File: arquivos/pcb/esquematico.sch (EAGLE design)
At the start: 14 parts, among them IC1 LM35CZ, IC2 LM35CZ, J1 694108210102, Q1 TIP31, Q2 TIP31

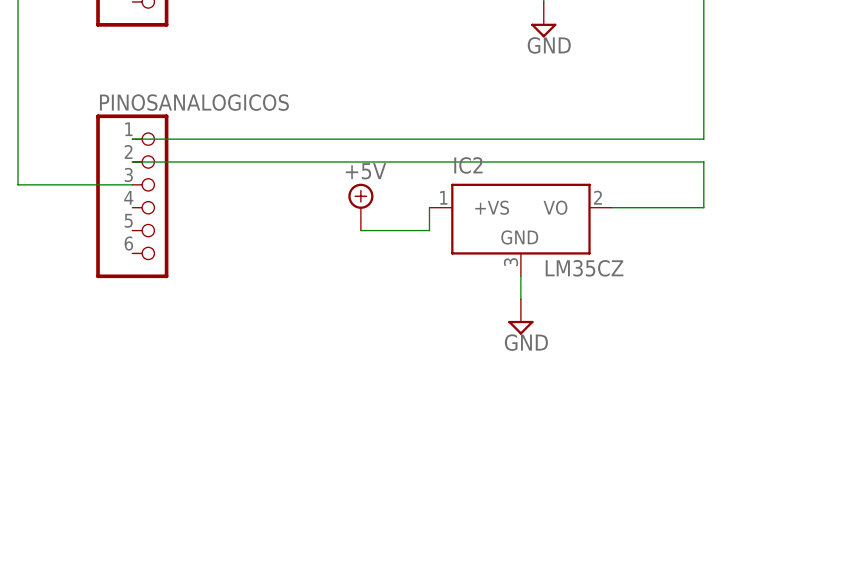
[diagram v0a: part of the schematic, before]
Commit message: Esquematico atualizado
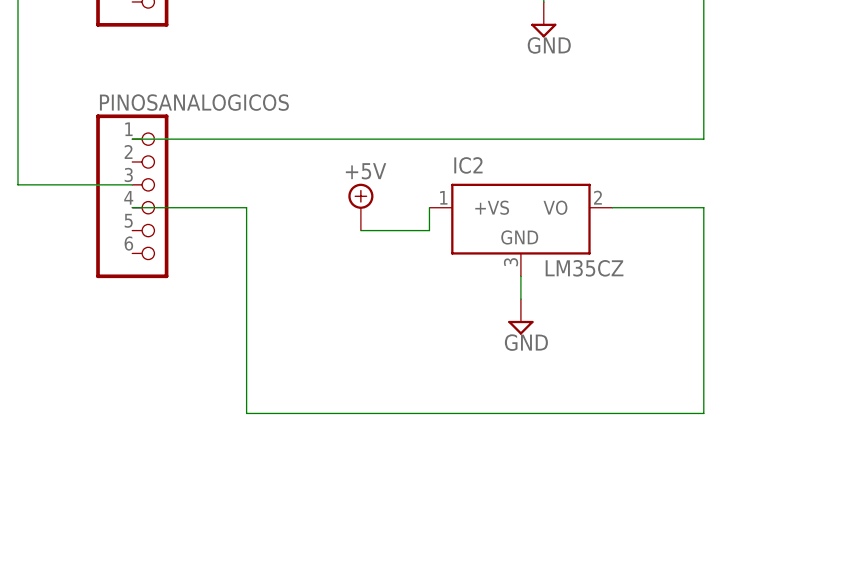
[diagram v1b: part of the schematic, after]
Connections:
- net N$1: now also PINOSANALOGICOS.4; no longer PINOSANALOGICOS.2
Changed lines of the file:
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@@
 <pinref part="IC2" gate="G$1" pin="VO"/>
 <wire x1="35.56" y1="5.08" x2="45.72" y2="5.08" width="0.1524" layer="91"/>
-<pinref part="PINOSANALOGICOS" gate="A" pin="2"/>
-<wire x1="45.72" y1="5.08" x2="45.72" y2="10.16" width="0.1524" layer="91"/>
-<wire x1="45.72" y1="10.16" x2="-17.78" y2="10.16" width="0.1524" layer="91"/>
+<wire x1="45.72" y1="5.08" x2="45.72" y2="-17.78" width="0.1524" layer="91"/>
+<wire x1="45.72" y1="-17.78" x2="-5.08" y2="-17.78" width="0.1524" layer="91"/>
+<wire x1="-5.08" y1="-17.78" x2="-5.08" y2="5.08" width="0.1524" layer="91"/>
+<pinref part="PINOSANALOGICOS" gate="A" pin="4"/>
+<wire x1="-5.08" y1="5.08" x2="-17.78" y2="5.08" width="0.1524" layer="91"/>
 </segment>
 </net>
-<net name="N$5" class="0">
+<net name="N$14" class="0">
 <segment>
 <pinref part="IC1" gate="G$1" pin="VO"/>
